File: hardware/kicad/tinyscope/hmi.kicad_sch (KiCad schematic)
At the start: 61 parts, among them J8 Waveshare 16498

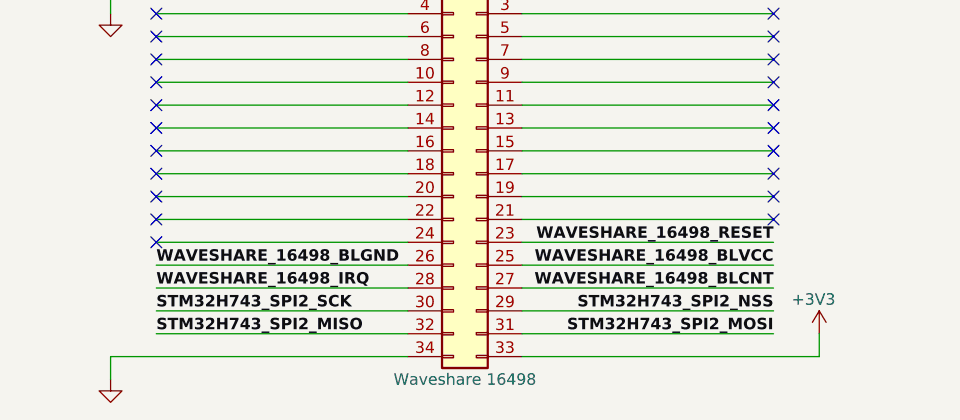
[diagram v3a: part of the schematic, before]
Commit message: fix: hardware: Solves electrical rules warnings and errors #7
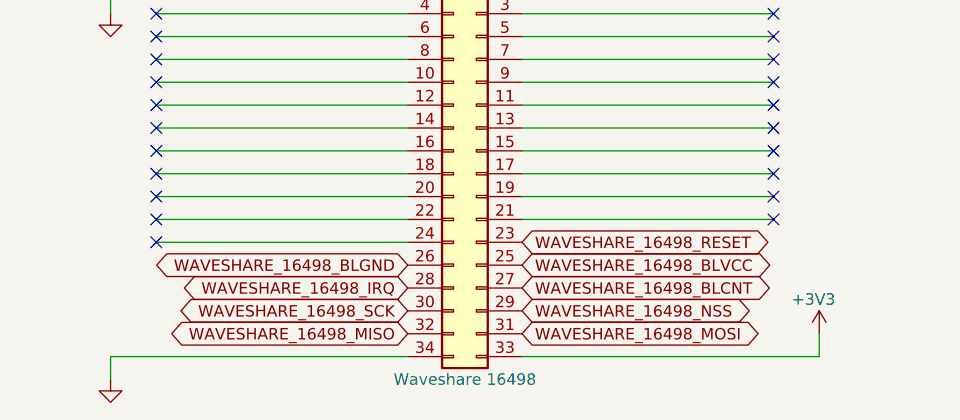
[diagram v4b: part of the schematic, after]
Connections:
- net STM32H743_SPI2_MISO renamed WAVESHARE_16498_MISO
- net STM32H743_SPI2_MOSI renamed WAVESHARE_16498_MOSI
- net STM32H743_SPI2_NSS renamed WAVESHARE_16498_NSS
- net STM32H743_SPI2_SCK renamed WAVESHARE_16498_SCK
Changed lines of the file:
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@@
-    (stroke (width 0) (type default))
-  )
-  (wire (pts (xy 68.58 175.26) (xy 96.52 175.26))
     (stroke (width 0) (type default))
   )
@@
     (stroke (width 0) (type default))
   )
-  (wire (pts (xy 68.58 177.8) (xy 96.52 177.8))
-    (stroke (width 0) (type default))
-  )
   (wire (pts (xy 53.34 58.42) (xy 53.34 60.96))
     (stroke (width 0) (type default))
@@
     (stroke (width 0) (type default))
   )
-  (wire (pts (xy 68.58 185.42) (xy 96.52 185.42))
-    (stroke (width 0) (type default))
-  )
   (wire (pts (xy 25.4 88.9) (xy 27.94 88.9))
     (stroke (width 0) (type default))
@@
     (stroke (width 0) (type default))
   )
-  (wire (pts (xy 68.58 182.88) (xy 96.52 182.88))
-    (stroke (width 0) (type default))
-  )
   (wire (pts (xy 50.8 116.84) (xy 50.8 119.38))
     (stroke (width 0) (type default))
@@
     (stroke (width 0) (type default))
   )
-  (wire (pts (xy 27.94 182.88) (xy 55.88 182.88))
-    (stroke (width 0) (type default))
-  )
   (wire (pts (xy 223.52 50.8) (xy 223.52 53.34))
     (stroke (width 0) (type default))
@@
     (stroke (width 0) (type default))
   )
-  (wire (pts (xy 27.94 185.42) (xy 55.88 185.42))
-    (stroke (width 0) (type default))
-  )
   (wire (pts (xy 213.36 68.58) (xy 213.36 71.12))
     (stroke (width 0) (type default))
@@
     (stroke (width 0) (type default))
   )
-  (wire (pts (xy 27.94 180.34) (xy 55.88 180.34))
-    (stroke (width 0) (type default))
-  )
   (wire (pts (xy 27.94 154.94) (xy 55.88 154.94))
     (stroke (width 0) (type default))
@@
     (stroke (width 0) (type default))
   )
-  (wire (pts (xy 68.58 180.34) (xy 96.52 180.34))
-    (stroke (width 0) (type default))
-  )
   (wire (pts (xy 27.94 152.4) (xy 55.88 152.4))
     (stroke (width 0) (type default))
@@
   )
   (wire (pts (xy 129.54 27.94) (xy 129.54 30.48))
-    (stroke (width 0) (type default))
-  )
-  (wire (pts (xy 27.94 177.8) (xy 55.88 177.8))
     (stroke (width 0) (type default))
   )
@@
     (effects (font (size 1.27 1.27) (thickness 0.254) bold) (justify left top))
   )
-  (label "STM32H743_SPI2_NSS" (at 96.52 182.88 180) (fields_autoplaced)
-    (effects (font (size 1.27 1.27) bold) (justify right bottom))
-  )
-  (label "STM32H743_SPI2_MISO" (at 27.94 185.42 0) (fields_autoplaced)
-    (effects (font (size 1.27 1.27) bold) (justify left bottom))
-  )
-  (label "STM32H743_SPI2_MOSI" (at 96.52 185.42 180) (fields_autoplaced)
-    (effects (font (size 1.27 1.27) bold) (justify right bottom))
-  )
-  (label "WAVESHARE_16498_IRQ" (at 27.94 180.34 0) (fields_autoplaced)
-    (effects (font (size 1.27 1.27) bold) (justify left bottom))
-  )
-  (label "WAVESHARE_16498_BLCNT" (at 96.52 180.34 180) (fields_autoplaced)
-    (effects (font (size 1.27 1.27) bold) (justify right bottom))
-  )
-  (label "WAVESHARE_16498_RESET" (at 96.52 175.26 180) (fields_autoplaced)
-    (effects (font (size 1.27 1.27) bold) (justify right bottom))
-  )
-  (label "STM32H743_SPI2_SCK" (at 27.94 182.88 0) (fields_autoplaced)
-    (effects (font (size 1.27 1.27) bold) (justify left bottom))
-  )
-  (label "WAVESHARE_16498_BLGND" (at 27.94 177.8 0) (fields_autoplaced)
-    (effects (font (size 1.27 1.27) bold) (justify left bottom))
-  )
-  (label "WAVESHARE_16498_BLVCC" (at 96.52 177.8 180) (fields_autoplaced)
-    (effects (font (size 1.27 1.27) bold) (justify right bottom))
-  )
   (global_label "ENC2_SW" (shape bidirectional) (at 119.38 30.48 180) (fields_autoplaced)
     (effects (font (size 1.27 1.27)) (justify right))
     (property "Intersheetrefs" "${INTERSHEET_REFS}" (at 106.7754 30.48 0)
+      (effects (font (size 1.27 1.27)) (justify right) hide)
+    )
+  )
+  (global_label "WAVESHARE_16498_BLGND" (shape bidirectional) (at 55.88 177.8 180) (fields_autoplaced)
+    (effects (font (size 1.27 1.27)) (justify right))
+    (property "Intersheetrefs" "${INTERSHEET_REFS}" (at 26.8864 177.8 0)
       (effects (font (size 1.27 1.27)) (justify right) hide)
     )
@@
     )
   )
+  (global_label "WAVESHARE_16498_SCK" (shape bidirectional) (at 55.88 182.88 180) (fields_autoplaced)
+    (effects (font (size 1.27 1.27)) (justify right))
+    (property "Intersheetrefs" "${INTERSHEET_REFS}" (at 29.3055 182.88 0)
+      (effects (font (size 1.27 1.27)) (justify right) hide)
+    )
+  )
   (global_label "ENC6_A" (shape bidirectional) (at 213.36 119.38 180) (fields_autoplaced)
     (effects (font (size 1.27 1.27)) (justify right))
     (property "Intersheetrefs" "${INTERSHEET_REFS}" (at 202.3277 119.38 0)
       (effects (font (size 1.27 1.27)) (justify right) hide)
+    )
+  )
+  (global_label "WAVESHARE_16498_NSS" (shape bidirectional) (at 68.58 182.88 0) (fields_autoplaced)
+    (effects (font (size 1.27 1.27)) (justify left))
+    (property "Intersheetrefs" "${INTERSHEET_REFS}" (at 95.1545 182.88 0)
+      (effects (font (size 1.27 1.27)) (justify left) hide)
     )
   )
@@
     )
   )
+  (global_label "WAVESHARE_16498_MISO" (shape bidirectional) (at 55.88 185.42 180) (fields_autoplaced)
+    (effects (font (size 1.27 1.27)) (justify right))
+    (property "Intersheetrefs" "${INTERSHEET_REFS}" (at 28.4588 185.42 0)
+      (effects (font (size 1.27 1.27)) (justify right) hide)
+    )
+  )
+  (global_label "WAVESHARE_16498_BLCNT" (shape bidirectional) (at 68.58 180.34 0) (fields_autoplaced)
+    (effects (font (size 1.27 1.27)) (justify left))
+    (property "Intersheetrefs" "${INTERSHEET_REFS}" (at 97.2712 180.34 0)
+      (effects (font (size 1.27 1.27)) (justify left) hide)
+    )
+  )
   (global_label "ENC1_A" (shape bidirectional) (at 25.4 60.96 180) (fields_autoplaced)
     (effects (font (size 1.27 1.27)) (justify right))
@@
     )
   )
+  (global_label "WAVESHARE_16498_BLVCC" (shape bidirectional) (at 68.58 177.8 0) (fields_autoplaced)
+    (effects (font (size 1.27 1.27)) (justify left))
+    (property "Intersheetrefs" "${INTERSHEET_REFS}" (at 97.3317 177.8 0)
+      (effects (font (size 1.27 1.27)) (justify left) hide)
+    )
+  )
+  (global_label "WAVESHARE_16498_MOSI" (shape bidirectional) (at 68.58 185.42 0) (fields_autoplaced)
+    (effects (font (size 1.27 1.27)) (justify left))
+    (property "Intersheetrefs" "${INTERSHEET_REFS}" (at 96.0012 185.42 0)
+      (effects (font (size 1.27 1.27)) (justify left) hide)
+    )
+  )
   (global_label "ENC6_SW" (shape bidirectional) (at 213.36 88.9 180) (fields_autoplaced)
     (effects (font (size 1.27 1.27)) (justify right))
@@
     )
   )
+  (global_label "WAVESHARE_16498_IRQ" (shape bidirectional) (at 55.88 180.34 180) (fields_autoplaced)
+    (effects (font (size 1.27 1.27)) (justify right))
+    (property "Intersheetrefs" "${INTERSHEET_REFS}" (at 29.8497 180.34 0)
+      (effects (font (size 1.27 1.27)) (justify right) hide)
+    )
+  )
+  (global_label "WAVESHARE_16498_RESET" (shape bidirectional) (at 68.58 175.26 0) (fields_autoplaced)
+    (effects (font (size 1.27 1.27)) (justify left))
+    (property "Intersheetrefs" "${INTERSHEET_REFS}" (at 97.1501 175.26 0)
+      (effects (font (size 1.27 1.27)) (justify left) hide)
+    )
+  )

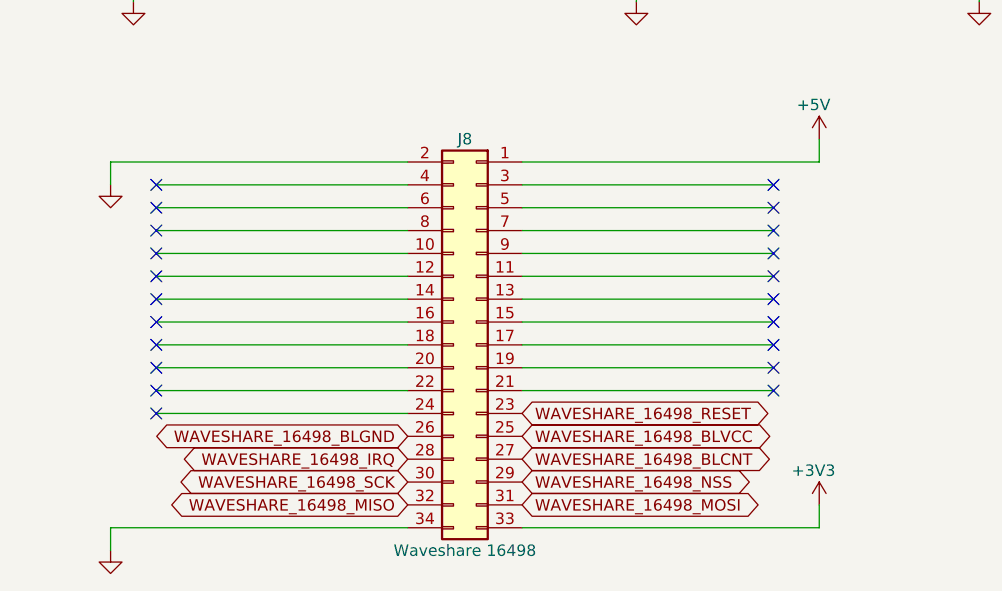
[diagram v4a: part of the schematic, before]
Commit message: fix: hardware: Solves electrical rules warnings and errors #9
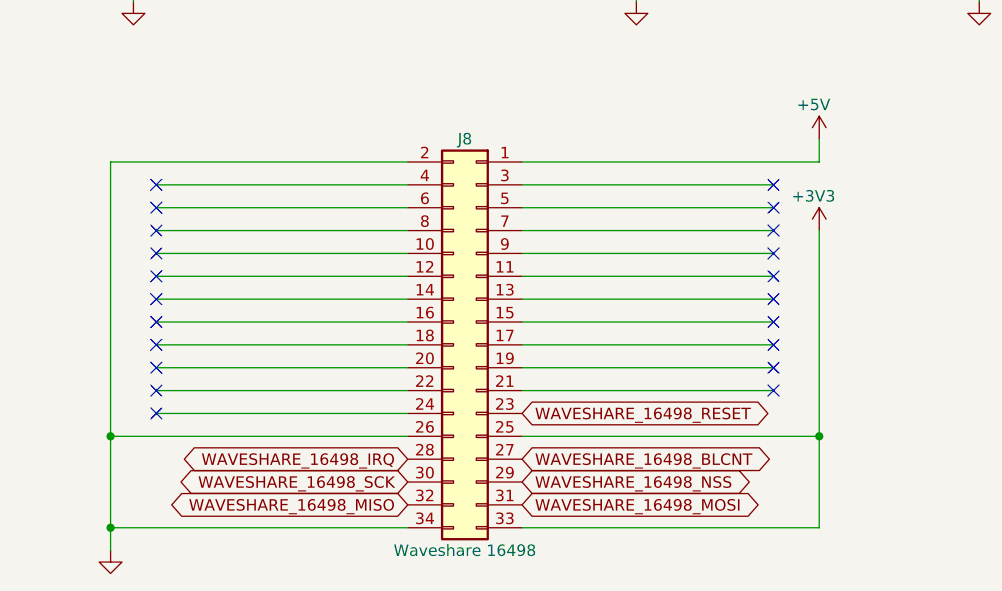
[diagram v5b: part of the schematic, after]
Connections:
- net WAVESHARE_16498_BLGND is gone; now on net GND: J8.26 (Pin_26)
- net WAVESHARE_16498_BLVCC is gone; now on net +3V3: J8.25 (Pin_25)
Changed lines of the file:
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@@
   (junction (at 35.56 88.9) (diameter 0) (color 0 0 0 0)
   )
+  (junction (at 22.86 177.8) (diameter 0) (color 0 0 0 0)
+  )
   (junction (at 223.52 30.48) (diameter 0) (color 0 0 0 0)
   )
@@
   (junction (at 71.12 119.38) (diameter 0) (color 0 0 0 0)
   )
+  (junction (at 101.6 177.8) (diameter 0) (color 0 0 0 0)
+  )
   (junction (at 35.56 119.38) (diameter 0) (color 0 0 0 0)
+  )
+  (junction (at 22.86 187.96) (diameter 0) (color 0 0 0 0)
   )
   (no_connect (at 66.04 45.72))
@@
     (stroke (width 0) (type default))
   )
+  (wire (pts (xy 68.58 177.8) (xy 101.6 177.8))
+    (stroke (width 0) (type default))
+  )
   (wire (pts (xy 25.4 40.64) (xy 25.4 43.18))
     (stroke (width 0) (type default))
@@
     (stroke (width 0) (type default))
   )
+  (wire (pts (xy 22.86 177.8) (xy 22.86 187.96))
+    (stroke (width 0) (type default))
+  )
   (wire (pts (xy 149.86 116.84) (xy 149.86 119.38))
     (stroke (width 0) (type default))
@@
     (stroke (width 0) (type default))
   )
+  (wire (pts (xy 101.6 177.8) (xy 101.6 187.96))
+    (stroke (width 0) (type default))
+  )
   (wire (pts (xy 238.76 91.44) (xy 238.76 88.9))
     (stroke (width 0) (type default))
@@
     (stroke (width 0) (type default))
   )
+  (wire (pts (xy 55.88 177.8) (xy 22.86 177.8))
+    (stroke (width 0) (type default))
+  )
   (wire (pts (xy 129.54 20.32) (xy 129.54 22.86))
     (stroke (width 0) (type default))
@@
     (stroke (width 0) (type default))
   )
-  (wire (pts (xy 22.86 147.32) (xy 22.86 149.86))
+  (wire (pts (xy 22.86 147.32) (xy 22.86 177.8))
     (stroke (width 0) (type default))
   )
@@
     (stroke (width 0) (type default))
   )
-  (wire (pts (xy 101.6 185.42) (xy 101.6 187.96))
+  (wire (pts (xy 101.6 154.94) (xy 101.6 177.8))
     (stroke (width 0) (type default))
   )
@@
     )
   )
-  (global_label "WAVESHARE_16498_BLGND" (shape bidirectional) (at 55.88 177.8 180) (fields_autoplaced)
-    (effects (font (size 1.27 1.27)) (justify right))
-    (property "Intersheetrefs" "${INTERSHEET_REFS}" (at 26.8864 177.8 0)
-      (effects (font (size 1.27 1.27)) (justify right) hide)
-    )
-  )
   (global_label "ENC1_B" (shape bidirectional) (at 81.28 60.96 0) (fields_autoplaced)
     (effects (font (size 1.27 1.27)) (justify left))
@@
     (property "Intersheetrefs" "${INTERSHEET_REFS}" (at 14.3677 60.96 0)
       (effects (font (size 1.27 1.27)) (justify right) hide)
-    )
-  )
-  (global_label "WAVESHARE_16498_BLVCC" (shape bidirectional) (at 68.58 177.8 0) (fields_autoplaced)
-    (effects (font (size 1.27 1.27)) (justify left))
-    (property "Intersheetrefs" "${INTERSHEET_REFS}" (at 97.3317 177.8 0)
-      (effects (font (size 1.27 1.27)) (justify left) hide)
     )
   )
@@
     )
   )
-  (symbol (lib_id "power:+3V3") (at 101.6 185.42 0) (mirror y) (unit 1)
-    (in_bom yes) (on_board yes) (dnp no)
-    (property "Reference" "#PWR041" (at 101.6 189.23 0)
-      (effects (font (size 1.27 1.27)) hide)
-    )
-    (property "Value" "+3V3" (at 100.965 181.61 0)
-      (effects (font (size 1.27 1.27)))
-    )
-    (property "Footprint" "" (at 101.6 185.42 0)
-      (effects (font (size 1.27 1.27)) hide)
-    )
-    (property "Datasheet" "" (at 101.6 185.42 0)
+  (symbol (lib_id "power:+3V3") (at 101.6 154.94 0) (mirror y) (unit 1)
+    (in_bom yes) (on_board yes) (dnp no)
+    (property "Reference" "#PWR041" (at 101.6 158.75 0)
+      (effects (font (size 1.27 1.27)) hide)
+    )
+    (property "Value" "+3V3" (at 100.965 151.13 0)
+      (effects (font (size 1.27 1.27)))
+    )
+    (property "Footprint" "" (at 101.6 154.94 0)
+      (effects (font (size 1.27 1.27)) hide)
+    )
+    (property "Datasheet" "" (at 101.6 154.94 0)
       (effects (font (size 1.27 1.27)) hide)
     )
@@
         )
       )
-    )
-  )
-  (symbol (lib_id "power:GND") (at 22.86 149.86 0) (mirror y) (unit 1)
-    (in_bom yes) (on_board yes) (dnp no) (fields_autoplaced)
-    (property "Reference" "#PWR?" (at 22.86 156.21 0)
-      (effects (font (size 1.27 1.27)) hide)
-    )
-    (property "Value" "GND" (at 22.86 154.94 0)
-      (effects (font (size 1.27 1.27)) hide)
-    )
-    (property "Footprint" "" (at 22.86 149.86 0)
-      (effects (font (size 1.27 1.27)) hide)
-    )
-    (property "Datasheet" "" (at 22.86 149.86 0)
-      (effects (font (size 1.27 1.27)) hide)
-    )
-    (pin "1")
-    (instances
-      (project "tinyscope"
-        (path "/bb072e32-cc57-415a-8554-0e84d374f333"
-          (reference "#PWR?") (unit 1)
-        )
-        (path "/bb072e32-cc57-415a-8554-0e84d374f333/1c26ba79-0794-42b8-82e1-265696d83365"
-          (reference "#PWR034") (unit 1)
-        )
-        (path "/bb072e32-cc57-415a-8554-0e84d374f333/f3c865ab-23cb-49a1-bb6d-4ee24e55c7fa"
-          (reference "#PWR052") (unit 1)
-        )
-        (path "/bb072e32-cc57-415a-8554-0e84d374f333/ef251a6f-7836-4e9b-b53d-220da1830612"
-          (reference "#PWR064") (unit 1)
-        )
-      )
